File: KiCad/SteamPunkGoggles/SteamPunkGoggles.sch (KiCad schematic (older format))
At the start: 7 parts

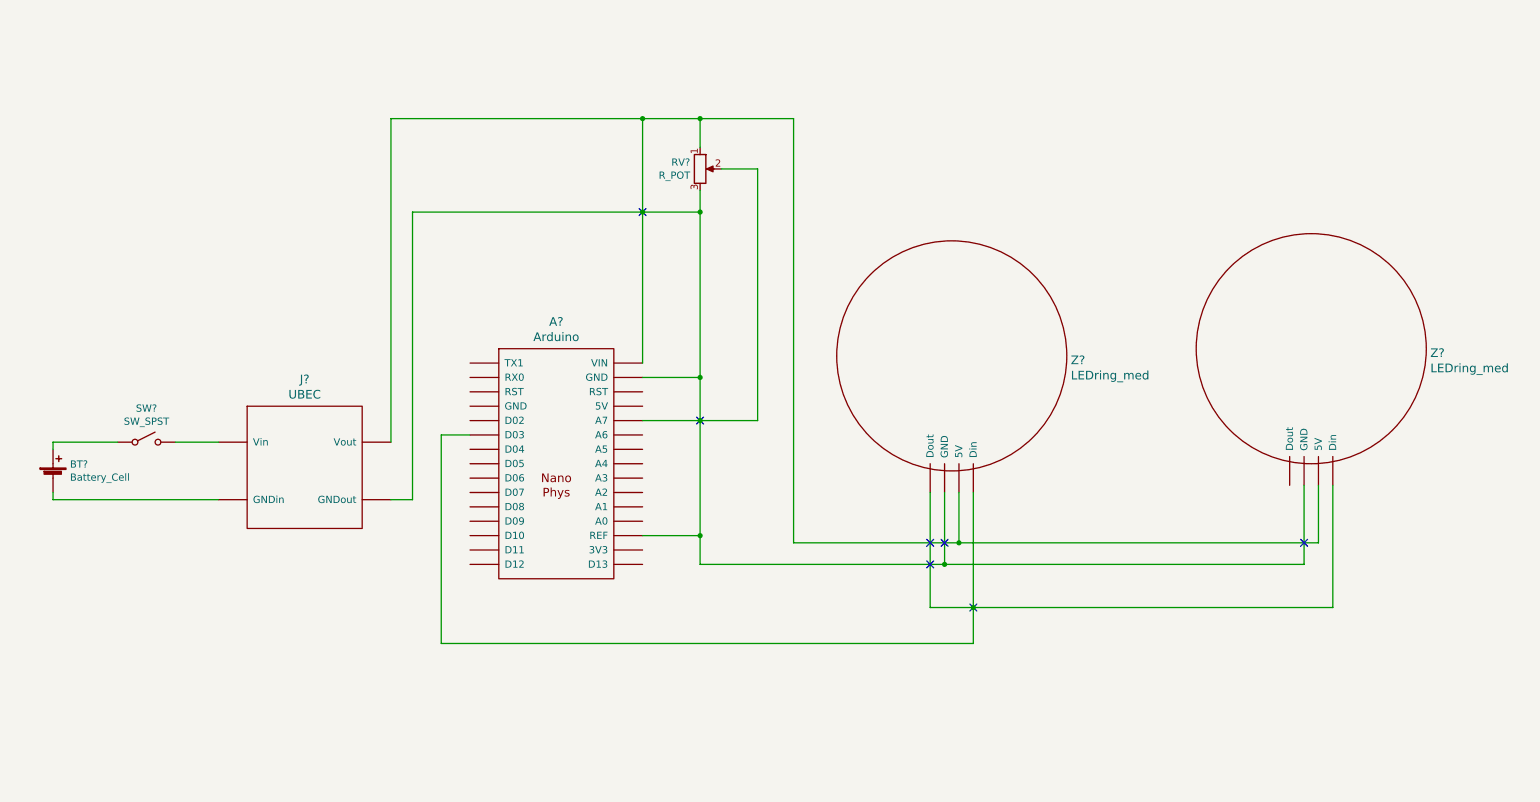
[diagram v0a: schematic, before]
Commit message: update schematic
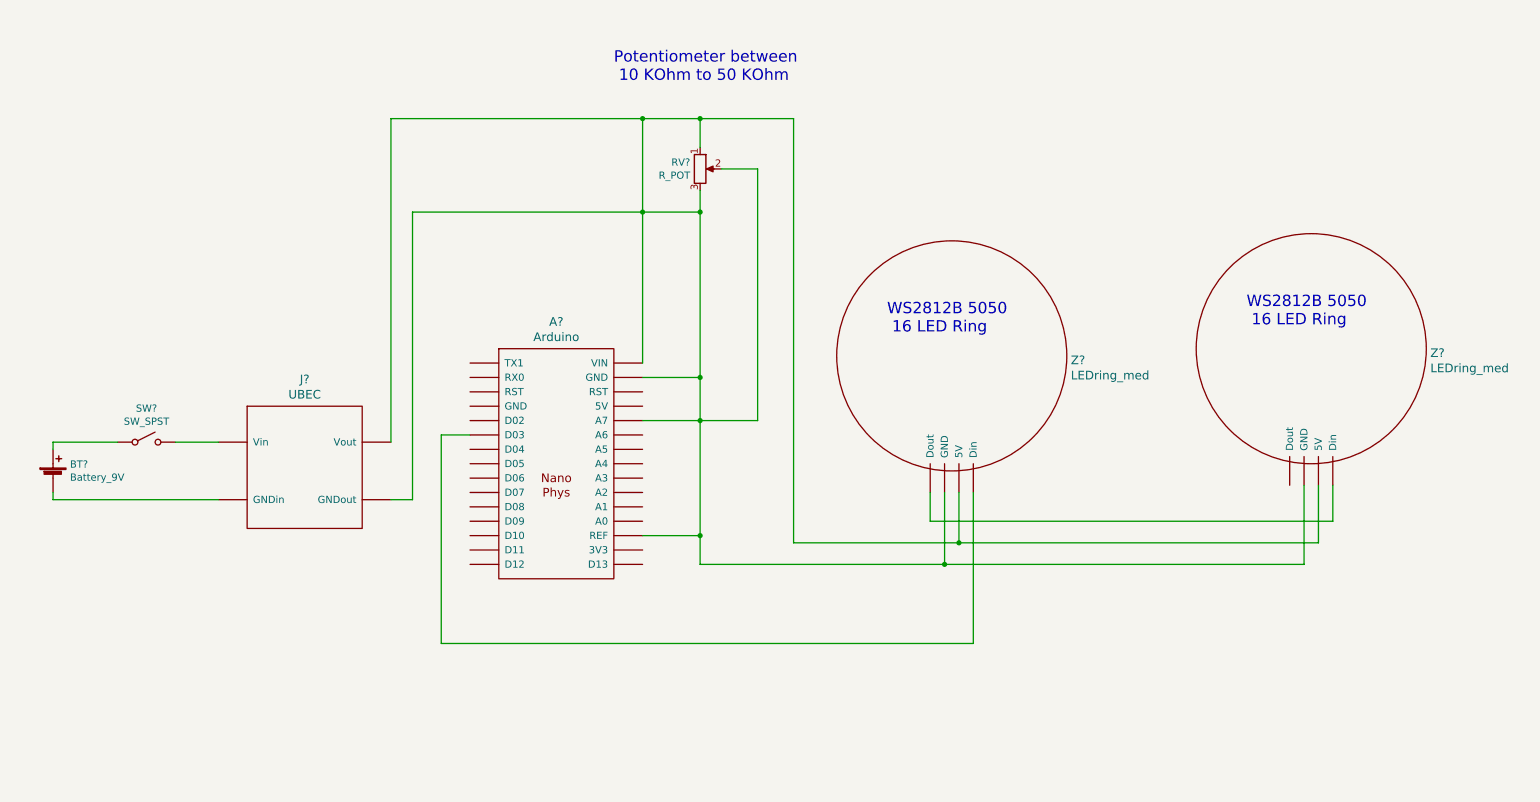
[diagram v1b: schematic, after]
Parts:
- BT?: value Battery_Cell -> Battery_9V
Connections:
- net at A?.~ (VIN): now also Z?.~ (GND)
- new net: A?.~ (VIN), J?.~ (Vout), RV?.1, RV?.2, RV?.3, Z?.~ (GND), Z?.~ (GND)
- new net: Z?.~ (GND), Z?.~ (GND)
- now unconnected: Z?.~ (GND), Z?.~ (GND)
- no-connect marks 7 -> 0
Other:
- note added: "Potentiometer between\n 10 KOhm to 50 KOhm"
- note added: "WS2812B 5050\n 16 LED Ring"
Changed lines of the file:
@@
 P 950 4050
 F 0 "BT?" H 1068 4146 50  0000 L CNN
-F 1 "Battery_Cell" H 1068 4055 50  0000 L CNN
+F 1 "Battery_9V" H 1068 4055 50  0000 L CNN
 F 2 "" V 950 4110 50  0001 C CNN
 F 3 "~" V 950 4110 50  0001 C CNN
@@
 	5450 4450 5050 4450
 Connection ~ 5450 3350
-NoConn ~ 5450 3650
-NoConn ~ 5050 2200
 Connection ~ 5050 2200
 Wire Wire Line
@@
 	950  4200 2100 4200
 Wire Wire Line
-	7050 4950 7350 4950
-Wire Wire Line
 	3650 5200 7350 5200
 Wire Wire Line
@@
 Wire Wire Line
 	6100 1550 6100 4500
-NoConn ~ 7350 4950
 $Comp
 L mdoLibrary:LEDring_med Z?
@@
 $EndComp
 Wire Wire Line
-	7350 5200 7350 4950
-Connection ~ 7350 4950
-Wire Wire Line
-	7350 4950 9850 4950
-Wire Wire Line
-	7350 4950 7350 4150
-Wire Wire Line
 	5450 4650 7150 4650
 Wire Wire Line
@@
 	7250 4500 9750 4500
 Wire Wire Line
-	7050 4150 7050 4950
-NoConn ~ 7050 4650
+	7050 4150 7050 4350
 Wire Wire Line
 	6100 4500 7250 4500
@@
 	9750 4100 9750 4500
 Wire Wire Line
-	9850 4100 9850 4950
-NoConn ~ 9650 4500
-NoConn ~ 7050 4500
-NoConn ~ 7150 4500
+	9850 4100 9850 4350
+Text Notes 6750 3050 0    79   ~ 0
+WS2812B 5050\n 16 LED Ring
+Text Notes 9250 3000 0    79   ~ 0
+WS2812B 5050\n 16 LED Ring
+Text Notes 4850 1300 0    79   ~ 0
+Potentiometer between\n 10 KOhm to 50 KOhm
+Wire Wire Line
+	7050 4350 9850 4350
+Wire Wire Line
+	7350 4150 7350 5200
 $EndSCHEMATC

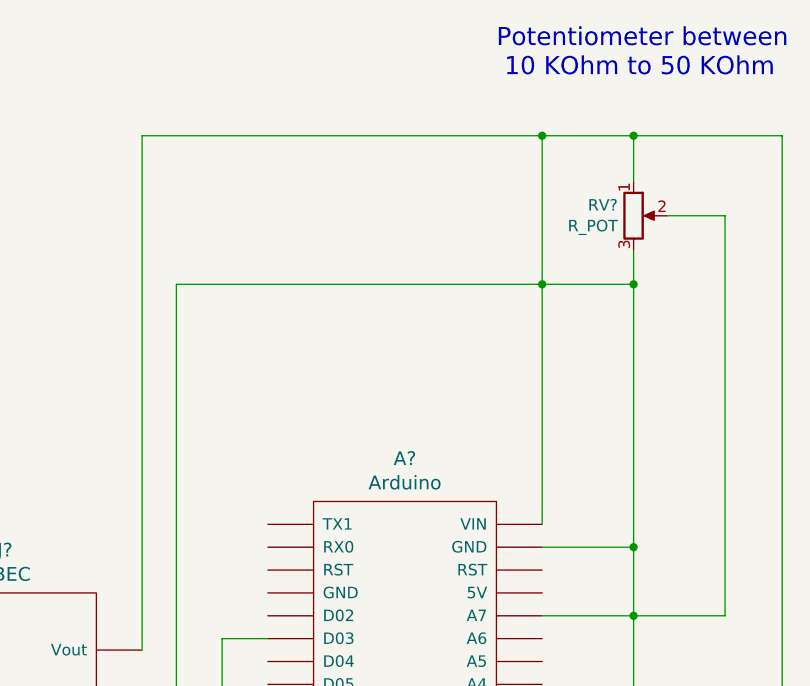
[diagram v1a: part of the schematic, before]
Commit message: update schematic
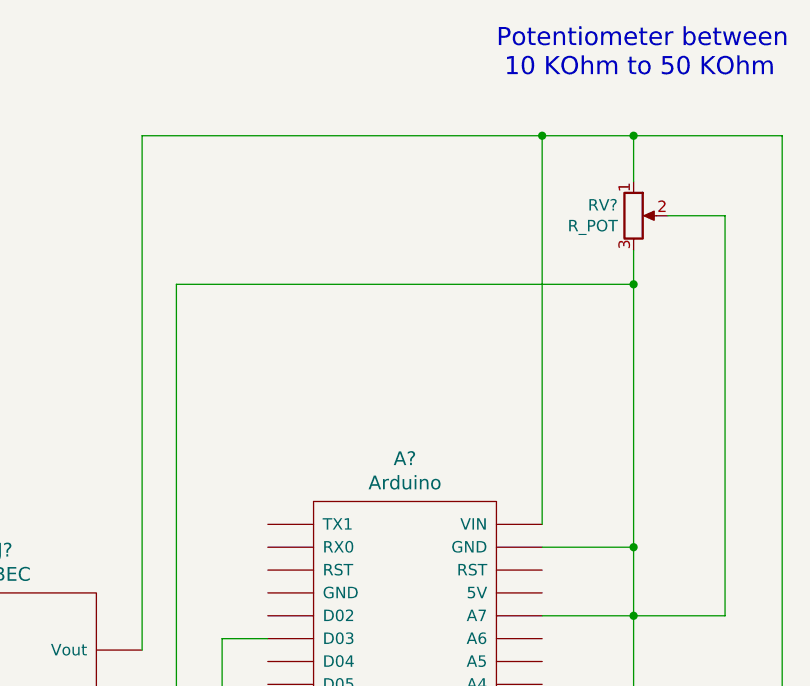
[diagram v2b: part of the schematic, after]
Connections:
- net at A?.~ (VIN): now also Z?.~ (GND)
- net at Z?.~ (GND): now also Z?.~ (GND); no longer A?.~ (VIN)
- net at Z?.~ (GND): no longer Z?.~ (GND)
- new net: A?.~ (VIN), J?.~ (Vout), RV?.1, Z?.~ (GND), Z?.~ (GND)
- new net: A?.~ (VIN), J?.~ (Vout), RV?.2, RV?.3, Z?.~ (GND), Z?.~ (GND)
- now unconnected: Z?.~ (GND)
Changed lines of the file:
@@
 Wire Wire Line
 	5450 2050 5450 2200
-Wire Wire Line
-	5050 3250 5050 2200
 Connection ~ 5450 2200
 Wire Wire Line
@@
 	5450 4450 5050 4450
 Connection ~ 5450 3350
-Connection ~ 5050 2200
-Wire Wire Line
-	5050 2200 5050 1550
-Wire Wire Line
-	5050 2200 5450 2200
 Connection ~ 5450 3650
 Wire Wire Line
@@
 Wire Wire Line
 	3450 2200 3450 4200
-Wire Wire Line
-	3450 2200 5050 2200
 Wire Wire Line
 	950  3800 950  3850
@@
 Wire Wire Line
 	7350 4150 7350 5200
+Wire Wire Line
+	5050 1550 5050 3250
+Wire Wire Line
+	3450 2200 5450 2200
 $EndSCHEMATC

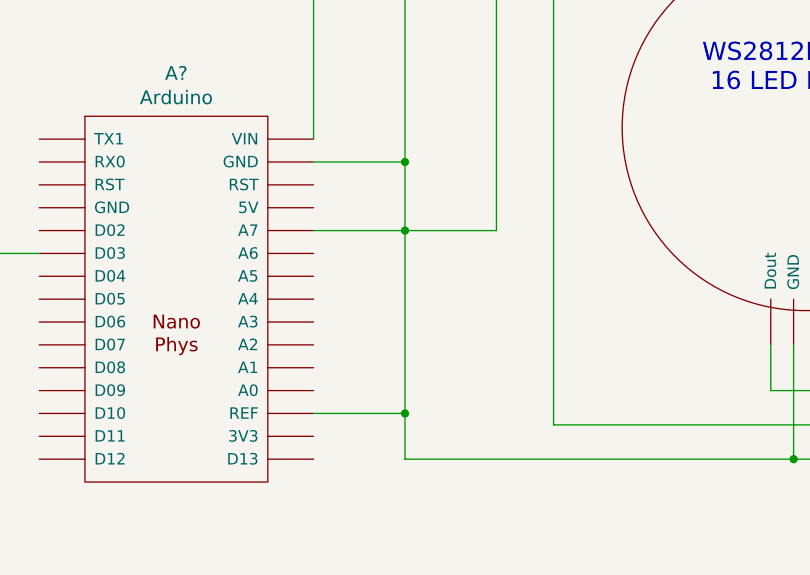
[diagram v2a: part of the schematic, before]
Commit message: update schematic
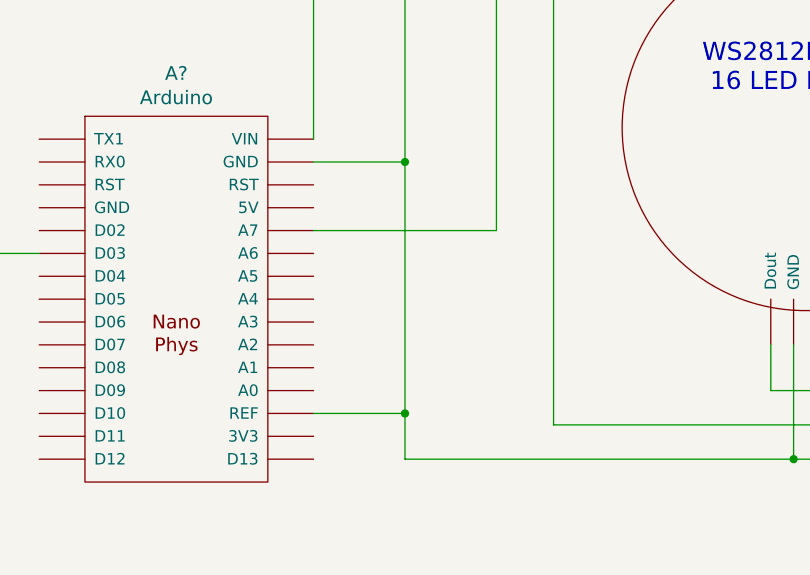
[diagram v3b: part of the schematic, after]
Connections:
- net at A?.~ (VIN): now also Z?.~ (GND)
- net at Z?.~ (GND): now also Z?.~ (GND); no longer A?.~ (VIN)
- net at Z?.~ (GND): no longer Z?.~ (GND)
- new net: A?.~ (VIN), J?.~ (Vout), RV?.1, Z?.~ (GND), Z?.~ (GND)
- new net: A?.~ (VIN), RV?.2
- new net: A?.~ (VIN), J?.~ (Vout), RV?.3, Z?.~ (GND), Z?.~ (GND)
- now unconnected: Z?.~ (GND), Z?.~ (GND)
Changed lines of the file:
@@
 	5850 1900 5850 3650
-Wire Wire Line
-	5850 3650 5450 3650
-Wire Wire Line
-	5450 3350 5450 3650
 Wire Wire Line
 	5450 4450 5050 4450
 Connection ~ 5450 3350
-Connection ~ 5450 3650
-Wire Wire Line
-	5450 3650 5050 3650
-Wire Wire Line
-	5450 3650 5450 4450
 Wire Wire Line
 	3850 3750 3650 3750
@@
 Wire Wire Line
 	3450 2200 5450 2200
+Wire Wire Line
+	5050 3650 5850 3650
+Wire Wire Line
+	5450 3350 5450 4450
 $EndSCHEMATC
